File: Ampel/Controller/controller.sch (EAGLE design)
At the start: 15 parts, among them IC1 ATtiny25, IC2 7805TV, X1 22-23-2041, X2 KUSBVX

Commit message: Stecker angepasst
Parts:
- removed X1: 22-23-2041, con-molex:22-23-2041
- added U$1: (no value), n39:PSW_5
- C3: value 470µ -> 47µ
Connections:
- net GND: now also U$1.GND1, U$1.GND2; no longer X1-2.S, X1-3.S
- net VCC: now also U$1.-5V; no longer X1-4.S
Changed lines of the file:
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@@
 <part name="GND1" library="supply1" deviceset="GND" device=""/>
 <part name="SUPPLY2" library="supply2" deviceset="VCC" device=""/>
-<part name="X1" library="con-molex" deviceset="22-23-2041" device=""/>
 <part name="GND3" library="supply1" deviceset="GND" device=""/>
 <part name="SUPPLY3" library="supply2" deviceset="VCC" device=""/>
@@
 <part name="GND4" library="supply1" deviceset="GND" device=""/>
 <part name="C2" library="resistor" deviceset="C-EU" device="025-024X044" value="0.1µ"/>
-<part name="C3" library="resistor" deviceset="CPOL-EU" device="E5-4" value="470µ"/>
+<part name="C3" library="resistor" deviceset="CPOL-EU" device="E5-4" value="47µ"/>
 <part name="D1" library="diode" deviceset="1N4004" device=""/>
 <part name="D2" library="diode" deviceset="1N4004" device=""/>
@@
 <part name="IC2" library="linear" deviceset="78*" device="TV" technology="05"/>
 <part name="JP1" library="pinhead" deviceset="PINHD-1X2" device=""/>
+<part name="U$1" library="n39" deviceset="PSW_5" device=""/>
 </parts>
 <sheets>
@@
 <instance part="GND1" gate="1" x="99.06" y="50.8"/>
 <instance part="SUPPLY2" gate="G$1" x="99.06" y="63.5"/>
-<instance part="X1" gate="-1" x="93.98" y="25.4"/>
-<instance part="X1" gate="-2" x="93.98" y="22.86"/>
-<instance part="X1" gate="-3" x="93.98" y="20.32"/>
-<instance part="X1" gate="-4" x="93.98" y="17.78"/>
 <instance part="GND3" gate="1" x="81.28" y="15.24"/>
-<instance part="SUPPLY3" gate="G$1" x="88.9" y="12.7" rot="R180"/>
+<instance part="SUPPLY3" gate="G$1" x="81.28" y="27.94" rot="R90"/>
 <instance part="OUT1" gate="G$1" x="33.02" y="-5.08" rot="R90"/>
 <instance part="OUT2" gate="G$1" x="50.8" y="-5.08" rot="R90"/>
@@
 <instance part="IC2" gate="A1" x="2.54" y="-22.86"/>
 <instance part="JP1" gate="G$1" x="-38.1" y="-27.94" rot="R180"/>
+<instance part="U$1" gate="G$1" x="93.98" y="20.32" rot="R90"/>
 </instances>
 <busses>
@@
 <segment>
 <pinref part="SUPPLY3" gate="G$1" pin="VCC"/>
-<wire x1="88.9" y1="15.24" x2="88.9" y2="17.78" width="0.1524" layer="91"/>
-<pinref part="X1" gate="-4" pin="S"/>
-<wire x1="88.9" y1="17.78" x2="91.44" y2="17.78" width="0.1524" layer="91"/>
+<pinref part="U$1" gate="G$1" pin="-5V"/>
+<wire x1="83.82" y1="27.94" x2="93.98" y2="27.94" width="0.1524" layer="91"/>
 </segment>
 <segment>
@@
 <segment>
 <pinref part="GND3" gate="1" pin="GND"/>
-<wire x1="81.28" y1="17.78" x2="81.28" y2="20.32" width="0.1524" layer="91"/>
-<pinref part="X1" gate="-3" pin="S"/>
-<wire x1="81.28" y1="20.32" x2="91.44" y2="20.32" width="0.1524" layer="91"/>
-<wire x1="81.28" y1="20.32" x2="81.28" y2="22.86" width="0.1524" layer="91"/>
-<junction x="81.28" y="20.32"/>
-<pinref part="X1" gate="-2" pin="S"/>
-<wire x1="81.28" y1="22.86" x2="91.44" y2="22.86" width="0.1524" layer="91"/>
+<wire x1="81.28" y1="17.78" x2="81.28" y2="22.86" width="0.1524" layer="91"/>
+<pinref part="U$1" gate="G$1" pin="GND2"/>
+<wire x1="81.28" y1="22.86" x2="93.98" y2="22.86" width="0.1524" layer="91"/>
+<pinref part="U$1" gate="G$1" pin="GND1"/>
+<wire x1="93.98" y1="17.78" x2="81.28" y2="17.78" width="0.1524" layer="91"/>
+<junction x="81.28" y="17.78"/>
 </segment>
 <segment>

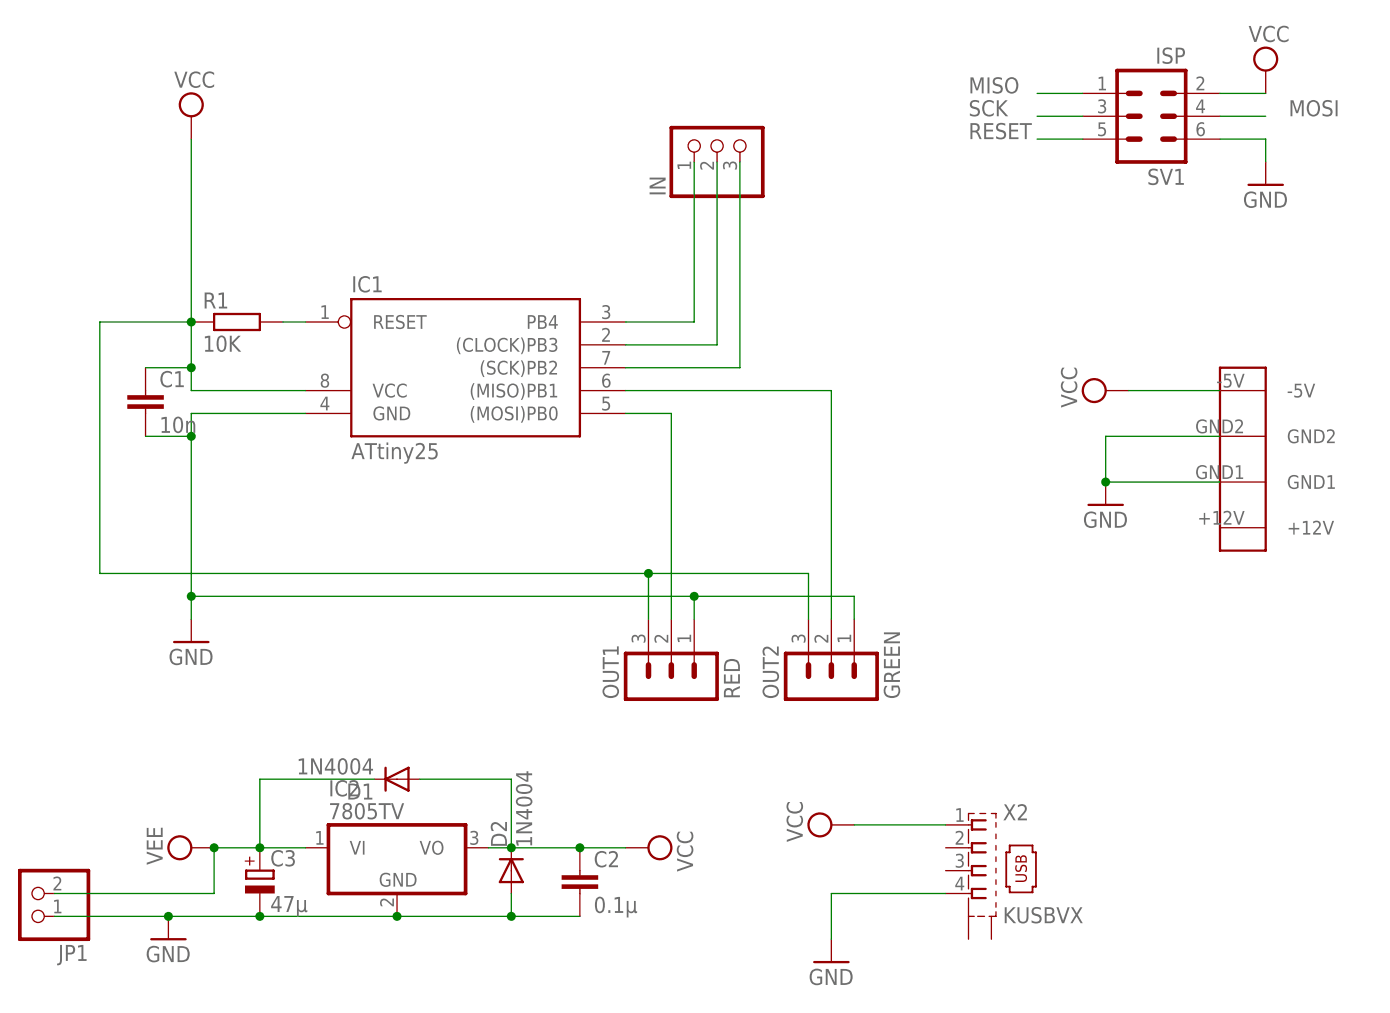
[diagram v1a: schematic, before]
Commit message: Redesign des Controller-Boards auf I2C
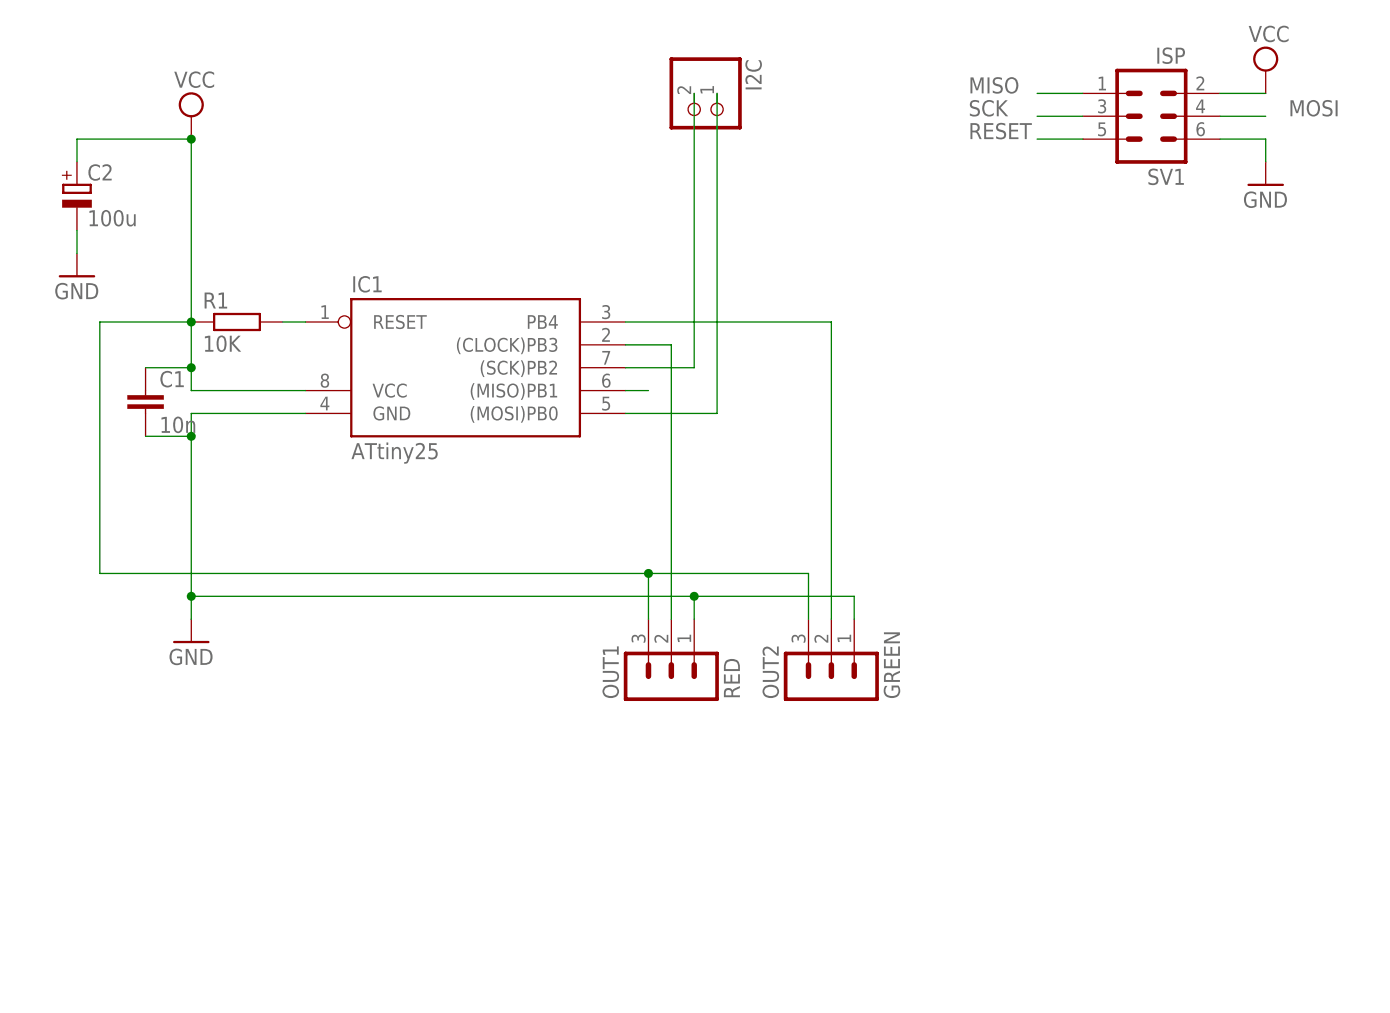
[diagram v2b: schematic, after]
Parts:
- removed C3: 47µ, resistor:CPOL-EUE5-4
- removed D1, D2: 1N4004, diode:1N4004
- removed IC2: 7805TV, linear:7805TV
- removed IN: (no value), pinhead:PINHD-1X3/90
- removed JP1: (no value), pinhead:PINHD-1X2
- removed U$1: (no value), n39:PSW_5
- removed X2: KUSBVX, con-kycon:KUSBVX
- added I2C: (no value), pinhead:PINHD-1X2
- C2: value 0.1µ -> 100u; device resistor:C-EU025-024X044 -> resistor:CPOL-EUE2.5-7
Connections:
- removed net VEE: C3.+, D1.C, IC2.VI, JP1.2
- net GND: now also C2.-; no longer C2.2, C3.-, D2.A, IC2.GND, JP1.1, U$1.GND1, U$1.GND2, X2.4
- net MISO: no longer OUT2.2
- net MOSI: now also I2C.1; no longer OUT1.2
- net N$1: now also IC1.PB4, OUT2.2; no longer IC1.(CLOCK)PB3, IN.2
- net N$2: now also IC1.(CLOCK)PB3, OUT1.2; no longer IC1.PB4, IN.1
- net SCK: now also I2C.2; no longer IN.3
- net VCC: now also C2.+; no longer C2.1, D1.A, D2.C, IC2.VO, U$1.-5V, X2.1
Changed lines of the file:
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@@
 <part name="GND1" library="supply1" deviceset="GND" device=""/>
 <part name="SUPPLY2" library="supply2" deviceset="VCC" device=""/>
-<part name="GND3" library="supply1" deviceset="GND" device=""/>
-<part name="SUPPLY3" library="supply2" deviceset="VCC" device=""/>
 <part name="OUT1" library="con-lstb" deviceset="MA03-1" device="" value="RED"/>
 <part name="OUT2" library="con-lstb" deviceset="MA03-1" device="" value="GREEN"/>
-<part name="IN" library="pinhead" deviceset="PINHD-1X3" device="/90"/>
-<part name="SUPPLY5" library="supply2" deviceset="VEE" device=""/>
-<part name="SUPPLY6" library="supply2" deviceset="VCC" device=""/>
-<part name="GND4" library="supply1" deviceset="GND" device=""/>
-<part name="C2" library="resistor" deviceset="C-EU" device="025-024X044" value="0.1µ"/>
-<part name="C3" library="resistor" deviceset="CPOL-EU" device="E5-4" value="47µ"/>
-<part name="D1" library="diode" deviceset="1N4004" device=""/>
-<part name="D2" library="diode" deviceset="1N4004" device=""/>
-<part name="X2" library="con-kycon" deviceset="KUSBVX" device=""/>
-<part name="SUPPLY7" library="supply2" deviceset="VCC" device=""/>
-<part name="GND5" library="supply1" deviceset="GND" device=""/>
-<part name="IC2" library="linear" deviceset="78*" device="TV" technology="05"/>
-<part name="JP1" library="pinhead" deviceset="PINHD-1X2" device=""/>
-<part name="U$1" library="n39" deviceset="PSW_5" device=""/>
+<part name="I2C" library="pinhead" deviceset="PINHD-1X2" device=""/>
+<part name="C2" library="resistor" deviceset="CPOL-EU" device="E2.5-7" value="100u"/>
+<part name="GND3" library="supply1" deviceset="GND" device=""/>
 </parts>
 <sheets>
@@
 <instance part="GND1" gate="1" x="99.06" y="50.8"/>
 <instance part="SUPPLY2" gate="G$1" x="99.06" y="63.5"/>
-<instance part="GND3" gate="1" x="81.28" y="15.24"/>
-<instance part="SUPPLY3" gate="G$1" x="81.28" y="27.94" rot="R90"/>
 <instance part="OUT1" gate="G$1" x="33.02" y="-5.08" rot="R90"/>
 <instance part="OUT2" gate="G$1" x="50.8" y="-5.08" rot="R90"/>
-<instance part="IN" gate="A" x="38.1" y="55.88" rot="R90"/>
-<instance part="SUPPLY5" gate="G$1" x="-20.32" y="-22.86" rot="R90"/>
-<instance part="SUPPLY6" gate="G$1" x="30.48" y="-22.86" rot="R270"/>
-<instance part="GND4" gate="1" x="-22.86" y="-33.02"/>
-<instance part="C2" gate="G$1" x="22.86" y="-25.4"/>
-<instance part="C3" gate="G$1" x="-12.7" y="-25.4"/>
-<instance part="D1" gate="1" x="2.54" y="-15.24" rot="R180"/>
-<instance part="D2" gate="1" x="15.24" y="-25.4" rot="R90"/>
-<instance part="X2" gate="G$1" x="68.58" y="-25.4"/>
-<instance part="SUPPLY7" gate="G$1" x="50.8" y="-20.32" rot="R90"/>
-<instance part="GND5" gate="1" x="50.8" y="-35.56"/>
-<instance part="IC2" gate="A1" x="2.54" y="-22.86"/>
-<instance part="JP1" gate="G$1" x="-38.1" y="-27.94" rot="R180"/>
-<instance part="U$1" gate="G$1" x="93.98" y="20.32" rot="R90"/>
+<instance part="I2C" gate="G$1" x="35.56" y="58.42" rot="R270"/>
+<instance part="C2" gate="G$1" x="-33.02" y="50.8"/>
+<instance part="GND3" gate="1" x="-33.02" y="40.64"/>
 </instances>
 <busses>
@@
 <wire x1="-30.48" y1="7.62" x2="-30.48" y2="35.56" width="0.1524" layer="91"/>
 <wire x1="-30.48" y1="35.56" x2="-20.32" y2="35.56" width="0.1524" layer="91"/>
+<pinref part="C2" gate="G$1" pin="+"/>
+<wire x1="-33.02" y1="53.34" x2="-33.02" y2="55.88" width="0.1524" layer="91"/>
+<wire x1="-33.02" y1="55.88" x2="-20.32" y2="55.88" width="0.1524" layer="91"/>
+<junction x="-20.32" y="55.88"/>
 </segment>
 <segment>
@@
 <wire x1="93.98" y1="60.96" x2="99.06" y2="60.96" width="0.1524" layer="91"/>
 <pinref part="SUPPLY2" gate="G$1" pin="VCC"/>
-</segment>
-<segment>
-<pinref part="SUPPLY3" gate="G$1" pin="VCC"/>
-<pinref part="U$1" gate="G$1" pin="-5V"/>
-<wire x1="83.82" y1="27.94" x2="93.98" y2="27.94" width="0.1524" layer="91"/>
-</segment>
-<segment>
-<pinref part="SUPPLY6" gate="G$1" pin="VCC"/>
-<wire x1="12.7" y1="-22.86" x2="15.24" y2="-22.86" width="0.1524" layer="91"/>
-<pinref part="D2" gate="1" pin="C"/>
-<wire x1="15.24" y1="-22.86" x2="22.86" y2="-22.86" width="0.1524" layer="91"/>
-<wire x1="22.86" y1="-22.86" x2="27.94" y2="-22.86" width="0.1524" layer="91"/>
-<junction x="15.24" y="-22.86"/>
-<pinref part="C2" gate="G$1" pin="1"/>
-<junction x="22.86" y="-22.86"/>
-<pinref part="D1" gate="1" pin="A"/>
-<wire x1="5.08" y1="-15.24" x2="15.24" y2="-15.24" width="0.1524" layer="91"/>
-<wire x1="15.24" y1="-15.24" x2="15.24" y2="-22.86" width="0.1524" layer="91"/>
-<pinref part="IC2" gate="A1" pin="VO"/>
-</segment>
-<segment>
-<pinref part="X2" gate="G$1" pin="1"/>
-<pinref part="SUPPLY7" gate="G$1" pin="VCC"/>
-<wire x1="63.5" y1="-20.32" x2="53.34" y2="-20.32" width="0.1524" layer="91"/>
 </segment>
 </net>
@@
 <segment>
 <pinref part="GND3" gate="1" pin="GND"/>
-<wire x1="81.28" y1="17.78" x2="81.28" y2="22.86" width="0.1524" layer="91"/>
-<pinref part="U$1" gate="G$1" pin="GND2"/>
-<wire x1="81.28" y1="22.86" x2="93.98" y2="22.86" width="0.1524" layer="91"/>
-<pinref part="U$1" gate="G$1" pin="GND1"/>
-<wire x1="93.98" y1="17.78" x2="81.28" y2="17.78" width="0.1524" layer="91"/>
-<junction x="81.28" y="17.78"/>
-</segment>
-<segment>
-<pinref part="GND4" gate="1" pin="GND"/>
-<wire x1="-22.86" y1="-30.48" x2="-12.7" y2="-30.48" width="0.1524" layer="91"/>
-<pinref part="D2" gate="1" pin="A"/>
-<wire x1="15.24" y1="-27.94" x2="15.24" y2="-30.48" width="0.1524" layer="91"/>
-<pinref part="C3" gate="G$1" pin="-"/>
-<junction x="-12.7" y="-30.48"/>
-<wire x1="-12.7" y1="-30.48" x2="2.54" y2="-30.48" width="0.1524" layer="91"/>
-<pinref part="C2" gate="G$1" pin="2"/>
-<wire x1="2.54" y1="-30.48" x2="15.24" y2="-30.48" width="0.1524" layer="91"/>
-<wire x1="15.24" y1="-30.48" x2="22.86" y2="-30.48" width="0.1524" layer="91"/>
-<junction x="15.24" y="-30.48"/>
-<pinref part="IC2" gate="A1" pin="GND"/>
-<junction x="2.54" y="-30.48"/>
-<pinref part="JP1" gate="G$1" pin="1"/>
-<wire x1="-35.56" y1="-30.48" x2="-22.86" y2="-30.48" width="0.1524" layer="91"/>
-<junction x="-22.86" y="-30.48"/>
-</segment>
-<segment>
-<pinref part="X2" gate="G$1" pin="4"/>
-<wire x1="63.5" y1="-27.94" x2="50.8" y2="-27.94" width="0.1524" layer="91"/>
-<pinref part="GND5" gate="1" pin="GND"/>
-<wire x1="50.8" y1="-27.94" x2="50.8" y2="-33.02" width="0.1524" layer="91"/>
+<pinref part="C2" gate="G$1" pin="-"/>
+<wire x1="-33.02" y1="43.18" x2="-33.02" y2="45.72" width="0.1524" layer="91"/>
 </segment>
 </net>
@@
 <segment>
 <pinref part="IC1" gate="G$1" pin="(MISO)PB1"/>
-<pinref part="OUT2" gate="G$1" pin="2"/>
-<wire x1="50.8" y1="2.54" x2="50.8" y2="27.94" width="0.1524" layer="91"/>
-<wire x1="50.8" y1="27.94" x2="27.94" y2="27.94" width="0.1524" layer="91"/>
+<wire x1="27.94" y1="27.94" x2="30.48" y2="27.94" width="0.1524" layer="91"/>
 </segment>
 </net>
@@
 <segment>
 <pinref part="IC1" gate="G$1" pin="(SCK)PB2"/>
-<wire x1="27.94" y1="30.48" x2="40.64" y2="30.48" width="0.1524" layer="91"/>
-<pinref part="IN" gate="A" pin="3"/>
-<wire x1="40.64" y1="30.48" x2="40.64" y2="53.34" width="0.1524" layer="91"/>
+<wire x1="27.94" y1="30.48" x2="35.56" y2="30.48" width="0.1524" layer="91"/>
+<pinref part="I2C" gate="G$1" pin="2"/>
+<wire x1="35.56" y1="60.96" x2="35.56" y2="30.48" width="0.1524" layer="91"/>
 </segment>
 </net>
@@
 <segment>
 <pinref part="IC1" gate="G$1" pin="(MOSI)PB0"/>
-<wire x1="27.94" y1="25.4" x2="33.02" y2="25.4" width="0.1524" layer="91"/>
-<pinref part="OUT1" gate="G$1" pin="2"/>
-<wire x1="33.02" y1="2.54" x2="33.02" y2="25.4" width="0.1524" layer="91"/>
+<wire x1="27.94" y1="25.4" x2="38.1" y2="25.4" width="0.1524" layer="91"/>
+<pinref part="I2C" gate="G$1" pin="1"/>
+<wire x1="38.1" y1="25.4" x2="38.1" y2="60.96" width="0.1524" layer="91"/>
 </segment>
 </net>
 <net name="N$1" class="0">
 <segment>
-<pinref part="IC1" gate="G$1" pin="(CLOCK)PB3"/>
-<wire x1="27.94" y1="33.02" x2="38.1" y2="33.02" width="0.1524" layer="91"/>
-<pinref part="IN" gate="A" pin="2"/>
-<wire x1="38.1" y1="33.02" x2="38.1" y2="53.34" width="0.1524" layer="91"/>
+<pinref part="OUT2" gate="G$1" pin="2"/>
+<wire x1="50.8" y1="2.54" x2="50.8" y2="35.56" width="0.1524" layer="91"/>
+<pinref part="IC1" gate="G$1" pin="PB4"/>
+<wire x1="50.8" y1="35.56" x2="27.94" y2="35.56" width="0.1524" layer="91"/>
 </segment>
 </net>
 <net name="N$2" class="0">
 <segment>
-<pinref part="IC1" gate="G$1" pin="PB4"/>
-<wire x1="27.94" y1="35.56" x2="35.56" y2="35.56" width="0.1524" layer="91"/>
-<pinref part="IN" gate="A" pin="1"/>
-<wire x1="35.56" y1="35.56" x2="35.56" y2="53.34" width="0.1524" layer="91"/>
+<pinref part="OUT1" gate="G$1" pin="2"/>
+<wire x1="33.02" y1="2.54" x2="33.02" y2="33.02" width="0.1524" layer="91"/>
+<pinref part="IC1" gate="G$1" pin="(CLOCK)PB3"/>
+<wire x1="33.02" y1="33.02" x2="27.94" y2="33.02" width="0.1524" layer="91"/>
 </segment>
 </net>
-<net name="VEE" class="0">
-<segment>
-<pinref part="SUPPLY5" gate="G$1" pin="VEE"/>
-<wire x1="-17.78" y1="-22.86" x2="-12.7" y2="-22.86" width="0.1524" layer="91"/>
-<pinref part="C3" gate="G$1" pin="+"/>
-<wire x1="-12.7" y1="-22.86" x2="-7.62" y2="-22.86" width="0.1524" layer="91"/>
-<junction x="-12.7" y="-22.86"/>
-<pinref part="D1" gate="1" pin="C"/>
-<wire x1="0" y1="-15.24" x2="-12.7" y2="-15.24" width="0.1524" layer="91"/>
-<wire x1="-12.7" y1="-15.24" x2="-12.7" y2="-22.86" width="0.1524" layer="91"/>
-<pinref part="IC2" gate="A1" pin="VI"/>
-<pinref part="JP1" gate="G$1" pin="2"/>
-<wire x1="-35.56" y1="-27.94" x2="-17.78" y2="-27.94" width="0.1524" layer="91"/>
-<wire x1="-17.78" y1="-27.94" x2="-17.78" y2="-22.86" width="0.1524" layer="91"/>
-<junction x="-17.78" y="-22.86"/>
-</segment>
-</net>

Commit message: Anpassung an Anschluss vom I2C-Adapter
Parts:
- removed I2C: (no value), pinhead:PINHD-1X2
- added SV2: (no value), con-lstb:MA04-1
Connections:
- net GND: now also SV2.4
- net MOSI: now also SV2.1; no longer I2C.1
- net SCK: now also SV2.2; no longer I2C.2
- net VCC: now also SV2.3
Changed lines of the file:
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@@
 <part name="OUT1" library="con-lstb" deviceset="MA03-1" device="" value="RED"/>
 <part name="OUT2" library="con-lstb" deviceset="MA03-1" device="" value="GREEN"/>
-<part name="I2C" library="pinhead" deviceset="PINHD-1X2" device=""/>
 <part name="C2" library="resistor" deviceset="CPOL-EU" device="E2.5-7" value="100u"/>
 <part name="GND3" library="supply1" deviceset="GND" device=""/>
+<part name="SV2" library="con-lstb" deviceset="MA04-1" device=""/>
+<part name="GND4" library="supply1" deviceset="GND" device=""/>
+<part name="SUPPLY3" library="supply2" deviceset="VCC" device=""/>
 </parts>
 <sheets>
@@
 <instance part="OUT1" gate="G$1" x="33.02" y="-5.08" rot="R90"/>
 <instance part="OUT2" gate="G$1" x="50.8" y="-5.08" rot="R90"/>
-<instance part="I2C" gate="G$1" x="35.56" y="58.42" rot="R270"/>
 <instance part="C2" gate="G$1" x="-33.02" y="50.8"/>
 <instance part="GND3" gate="1" x="-33.02" y="40.64"/>
+<instance part="SV2" gate="1" x="71.12" y="25.4"/>
+<instance part="GND4" gate="1" x="83.82" y="38.1" rot="R180"/>
+<instance part="SUPPLY3" gate="G$1" x="86.36" y="25.4" rot="R270"/>
 </instances>
 <busses>
@@
 <pinref part="SUPPLY2" gate="G$1" pin="VCC"/>
 </segment>
+<segment>
+<pinref part="SUPPLY3" gate="G$1" pin="VCC"/>
+<pinref part="SV2" gate="1" pin="3"/>
+<wire x1="83.82" y1="25.4" x2="78.74" y2="25.4" width="0.1524" layer="91"/>
+</segment>
 </net>
 <net name="GND" class="0">
@@
 <pinref part="C2" gate="G$1" pin="-"/>
 <wire x1="-33.02" y1="43.18" x2="-33.02" y2="45.72" width="0.1524" layer="91"/>
+</segment>
+<segment>
+<pinref part="SV2" gate="1" pin="4"/>
+<pinref part="GND4" gate="1" pin="GND"/>
+<wire x1="78.74" y1="27.94" x2="83.82" y2="33.02" width="0.1524" layer="91"/>
+<wire x1="83.82" y1="33.02" x2="83.82" y2="35.56" width="0.1524" layer="91"/>
 </segment>
 </net>
@@
 <pinref part="IC1" gate="G$1" pin="(SCK)PB2"/>
 <wire x1="27.94" y1="30.48" x2="35.56" y2="30.48" width="0.1524" layer="91"/>
-<pinref part="I2C" gate="G$1" pin="2"/>
-<wire x1="35.56" y1="60.96" x2="35.56" y2="30.48" width="0.1524" layer="91"/>
+<wire x1="35.56" y1="30.48" x2="43.18" y2="22.86" width="0.1524" layer="91"/>
+<pinref part="SV2" gate="1" pin="2"/>
+<wire x1="43.18" y1="22.86" x2="78.74" y2="22.86" width="0.1524" layer="91"/>
 </segment>
 </net>
@@
 <pinref part="IC1" gate="G$1" pin="(MOSI)PB0"/>
 <wire x1="27.94" y1="25.4" x2="38.1" y2="25.4" width="0.1524" layer="91"/>
-<pinref part="I2C" gate="G$1" pin="1"/>
-<wire x1="38.1" y1="25.4" x2="38.1" y2="60.96" width="0.1524" layer="91"/>
+<wire x1="38.1" y1="25.4" x2="43.18" y2="20.32" width="0.1524" layer="91"/>
+<pinref part="SV2" gate="1" pin="1"/>
+<wire x1="43.18" y1="20.32" x2="78.74" y2="20.32" width="0.1524" layer="91"/>
 </segment>
 </net>
